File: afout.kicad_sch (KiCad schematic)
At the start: 24 parts, among them J2 Conn_Coaxial, Q1 2N2222A, Q2 2N2222A

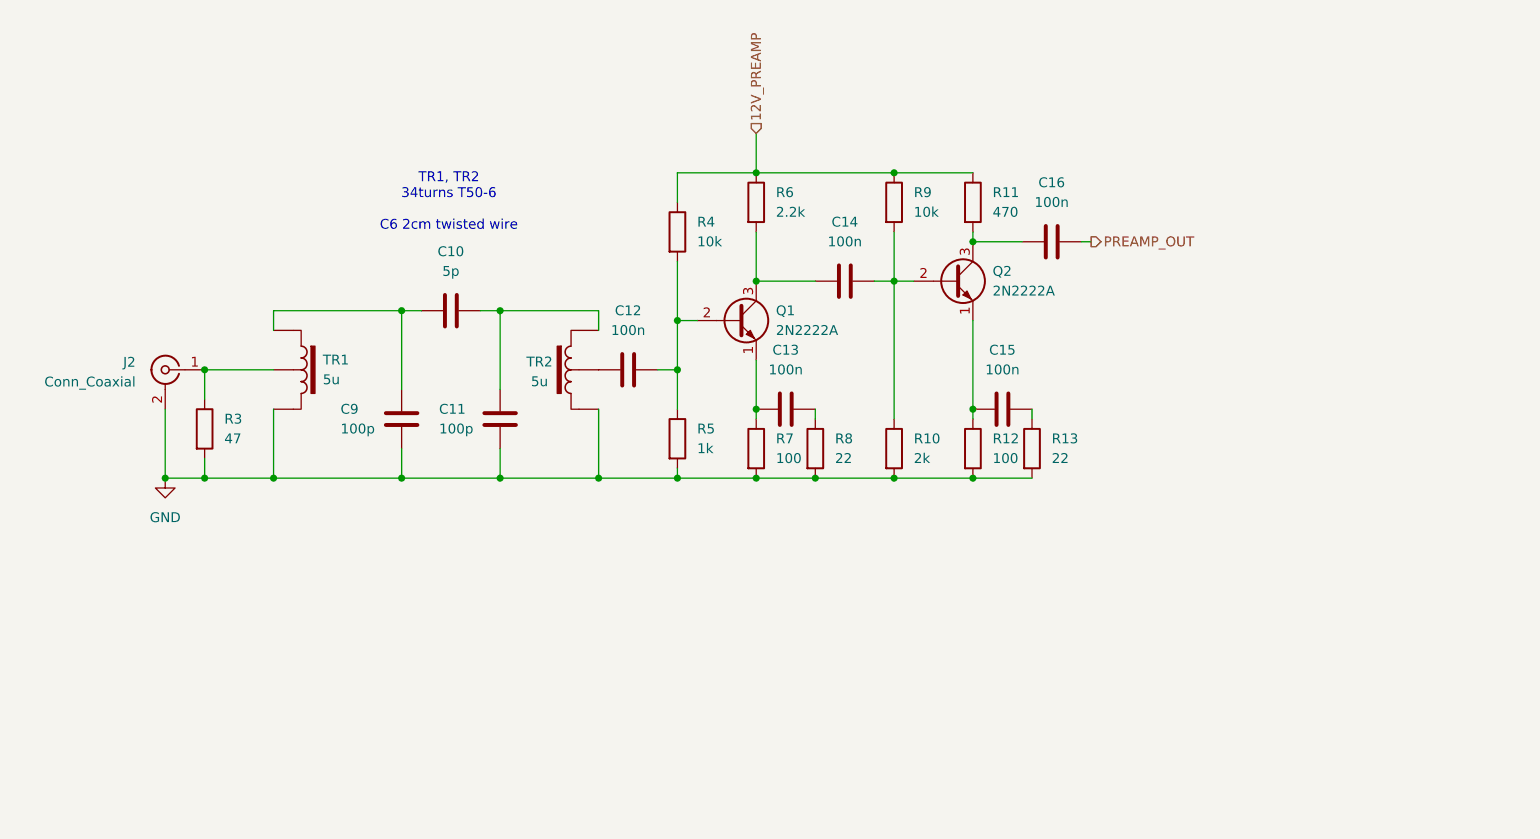
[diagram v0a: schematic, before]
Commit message: Rework RF amplifier design and add AF amplification
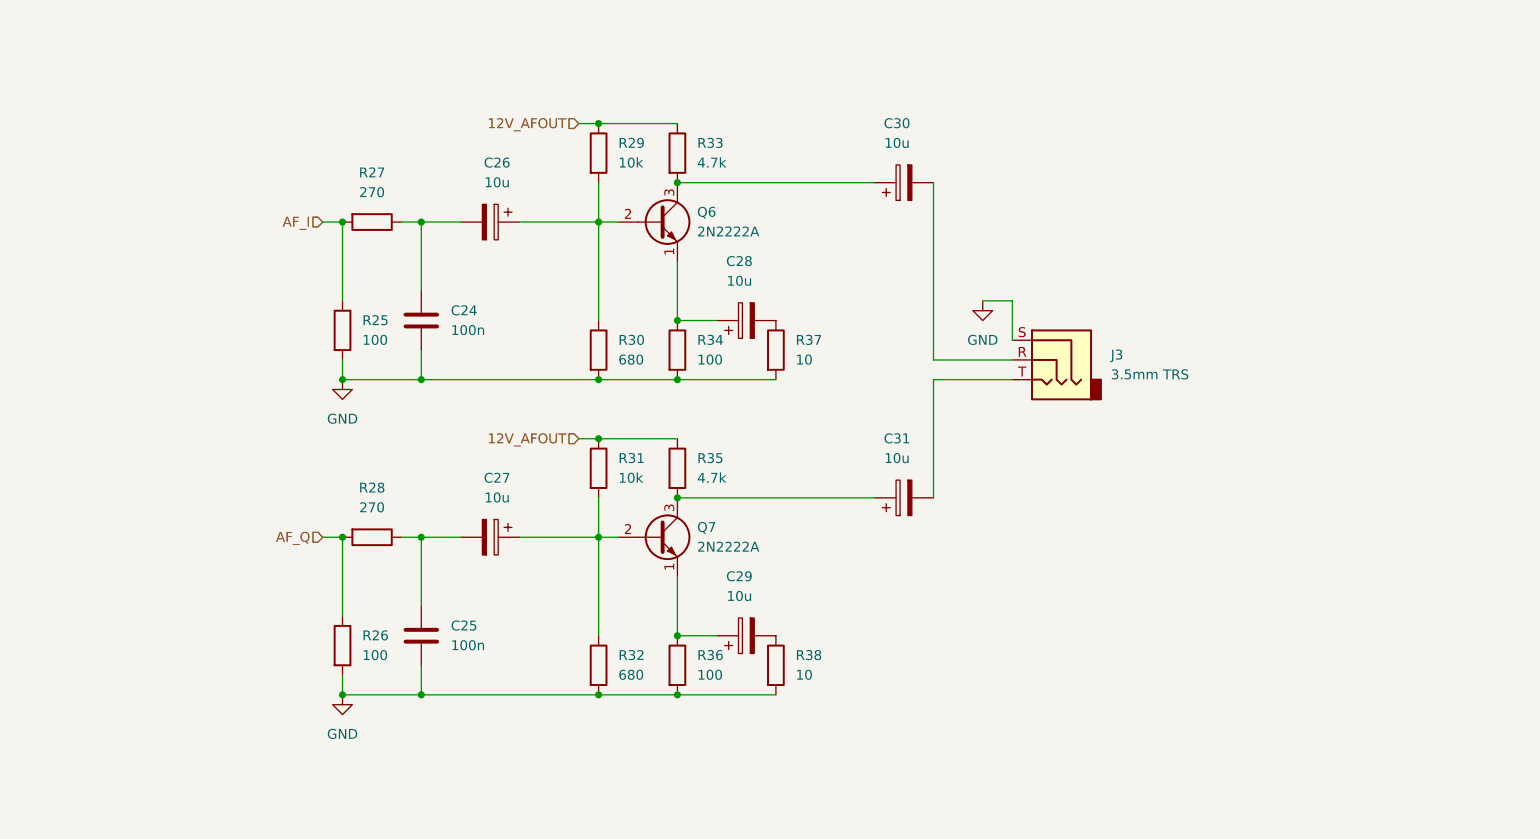
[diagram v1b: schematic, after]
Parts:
- removed C10: 5p, symbol Device:C
- removed C11, C9: 100p, symbol Device:C
- removed C12, C13, C14, C15, C16: 100n, symbol Device:C
- removed J2: Conn_Coaxial, symbol Connector:Conn_Coaxial
- removed Q1, Q2: 2N2222A, symbol Transistor_BJT:Q_NPN_EBC
- removed R10: 2k, symbol Device:R
- removed R11: 470, symbol Device:R
- removed R12, R7: 100, symbol Device:R
- removed R13, R8: 22, symbol Device:R
- removed R3: 47, symbol Device:R
- removed R4, R9: 10k, symbol Device:R
- removed R5: 1k, symbol Device:R
- removed R6: 2.2k, symbol Device:R
- removed TR1, TR2: 5u, symbol SDRLibrary:AUTOTRANSFORMER
- added C24, C25: 100n, symbol Device:C
- added C26, C27, C28, C29, C30, C31: 10u, symbol Device:C_Polarized
- added J3: 3.5mm TRS, symbol Connector_Audio:AudioJack3
- added Q6, Q7: 2N2222A, symbol Transistor_BJT:Q_NPN_EBC
- added R25, R26, R34, R36: 100, symbol Device:R
- added R27, R28: 270, symbol Device:R
- added R29, R31: 10k, symbol Device:R
- added R30, R32: 680, symbol Device:R
- added R33, R35: 4.7k, symbol Device:R
- added R37, R38: 10, symbol Device:R
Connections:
- net GND: now also C24.2, C25.2, J3.S, R25.2, R26.2, R30.2, R32.2, R34.2, R36.2, R37.2, R38.2
- new net: C30.1, Q6.3 (C), R33.2
- new net: C28.1, Q6.1 (E), R34.1
- new net: C25.1, C27.2, R28.1
- new net: C26.1, Q6.2 (B), R29.2, R30.1
- new net: C24.1, C26.2, R27.1
- new net: C29.1, Q7.1 (E), R36.1
- new net: C27.1, Q7.2 (B), R31.2, R32.1
- new net: C31.1, Q7.3 (C), R35.2
- new net: C30.2, J3.R
- new net: C31.2, J3.T
- new net: C29.2, R38.1
- new net: C28.2, R37.1
- new net 12V_AFOUT: R29.1, R31.1, R33.1, R35.1
- new net AF_I: R25.1, R27.2
- new net AF_Q: R26.1, R28.2
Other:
- note removed: "TR1, TR2 34turns T50-6 C6 2cm twisted wire"

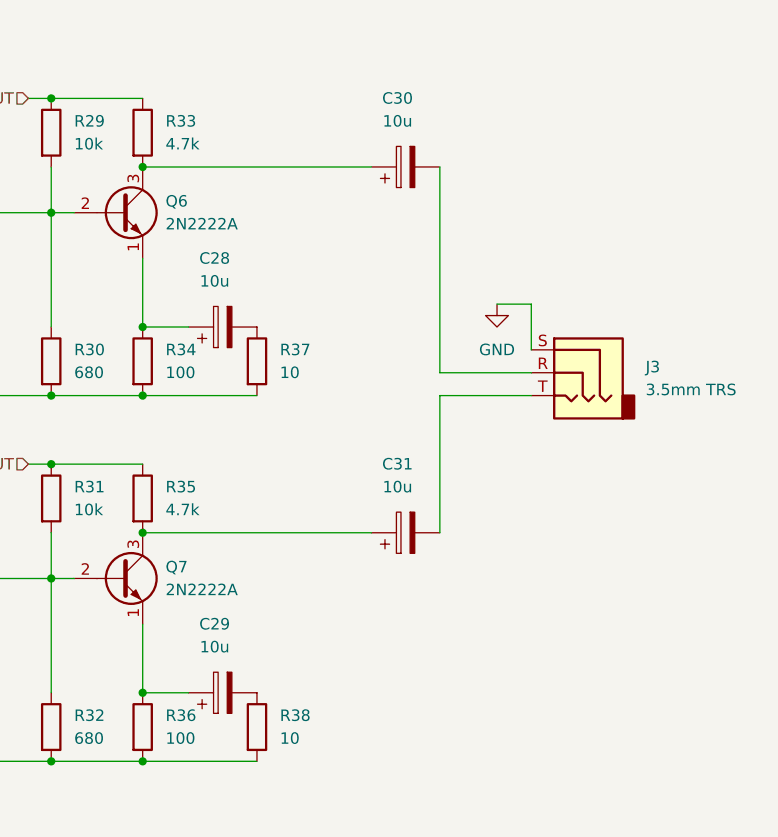
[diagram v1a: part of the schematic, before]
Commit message: Reduce AF gain, add clipping diodes
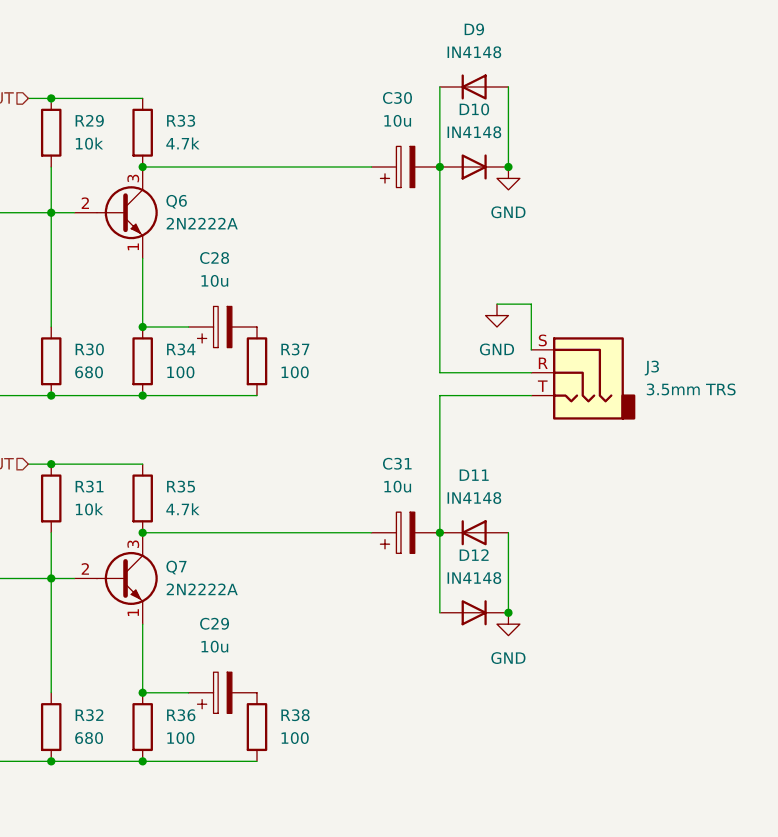
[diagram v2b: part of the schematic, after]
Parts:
- added D10, D11, D12, D9: IN4148, symbol Device:D
- R37, R38: value 10 -> 100
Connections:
- net GND: now also D10.1 (K), D11.2 (A), D12.1 (K), D9.2 (A)
- net at C30.2, J3.R: now also D10.2 (A), D9.1 (K)
- net at C31.2, J3.T: now also D11.1 (K), D12.2 (A)

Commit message: Add more gain fix crystal oscillator starting, add audio isolation transformers
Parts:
- added T5, T6: Transformer_SP_1S, symbol Device:Transformer_SP_1S
- R37, R38: value 100 -> 10
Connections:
- net GND: now also T5.3 (PR2), T6.1 (PR1); no longer J3.S
- net at C30.2, D10.2 (A), D9.1 (K): now also T5.1 (PR1); no longer J3.R
- net at C31.2, D11.1 (K), D12.2 (A): now also T6.3 (PR2); no longer J3.T
- new net: J3.S, T5.5 (S2), T6.4 (S1)
- new net: J3.T, T6.5 (S2)
- new net: J3.R, T5.4 (S1)
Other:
- moved on the sheet: C25, C27, C29, C31, D11, D12, J3, Q7, R26, R28, R31, R32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
